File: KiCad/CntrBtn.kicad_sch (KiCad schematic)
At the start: 3 parts

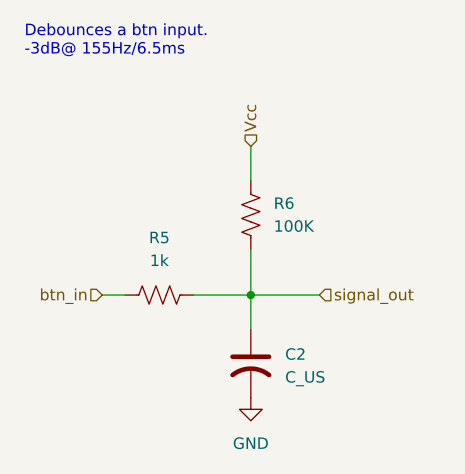
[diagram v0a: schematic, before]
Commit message: redid button pull up. Added initial joystick and display symbols
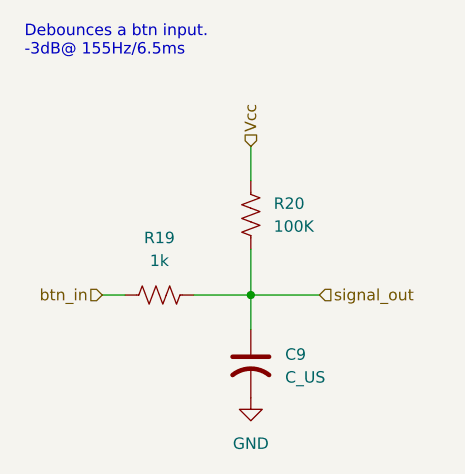
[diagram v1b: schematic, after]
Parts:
- renumbered C2 to C9, R5 to R19, R6 to R20
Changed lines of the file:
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@@
 		(dnp no)
 		(fields_autoplaced yes)
-		(property "Reference" "R5"
+		(property "Reference" "R19"
 			(at 38.1 45.72 90)
 			(effects
@@
 		(instances
 			(project "sb_handheld"
-				(path "/e2b47f54-afd4-414f-8c8f-251eedeb980e/77aafe8f-860d-4135-993b-3f03c481f100"
-					(reference "R5")
-					(unit 1)
-				)
 				(path "/e2b47f54-afd4-414f-8c8f-251eedeb980e/35c94761-efac-418a-91db-c9b83c0b3899/080458a5-8993-446e-83d9-bcde56d7c9a2"
 					(reference "R29")
@@
 				(path "/e2b47f54-afd4-414f-8c8f-251eedeb980e/35c94761-efac-418a-91db-c9b83c0b3899/f76cda86-381c-44b3-a7df-58f7c58efb05"
 					(reference "R31")
-					(unit 1)
-				)
-				(path "/e2b47f54-afd4-414f-8c8f-251eedeb980e/6239e351-1e9b-4e1a-998c-979da75b2bd8/2192cc8f-655d-4541-b277-b7a0a5260346"
-					(reference "R9")
-					(unit 1)
-				)
-				(path "/e2b47f54-afd4-414f-8c8f-251eedeb980e/6239e351-1e9b-4e1a-998c-979da75b2bd8/57806a10-d03e-45c2-905e-9ef24d9fc5a3"
-					(reference "R11")
-					(unit 1)
-				)
-				(path "/e2b47f54-afd4-414f-8c8f-251eedeb980e/6239e351-1e9b-4e1a-998c-979da75b2bd8/8ca35cf0-ef30-4af4-8c04-dbe73795e853"
-					(reference "R15")
-					(unit 1)
-				)
-				(path "/e2b47f54-afd4-414f-8c8f-251eedeb980e/6239e351-1e9b-4e1a-998c-979da75b2bd8/b6250329-bdc4-45c1-a6bb-2e0cadeb9f26"
-					(reference "R3")
-					(unit 1)
-				)
-				(path "/e2b47f54-afd4-414f-8c8f-251eedeb980e/6239e351-1e9b-4e1a-998c-979da75b2bd8/b65d468b-0271-475b-bfa0-5edddf91c73b"
-					(reference "R7")
-					(unit 1)
-				)
-				(path "/e2b47f54-afd4-414f-8c8f-251eedeb980e/6239e351-1e9b-4e1a-998c-979da75b2bd8/d2f4d4b1-81b0-4a1b-a44d-4fb0a202ecbb"
-					(reference "R17")
-					(unit 1)
-				)
-				(path "/e2b47f54-afd4-414f-8c8f-251eedeb980e/6239e351-1e9b-4e1a-998c-979da75b2bd8/d48abaaa-9c99-46dc-846f-bb3c471b4c2c"
-					(reference "R13")
 					(unit 1)
 				)
@@
 		(dnp no)
 		(fields_autoplaced yes)
-		(property "Reference" "#PWR030"
+		(property "Reference" "#PWR067"
 			(at 48.26 69.85 0)
 			(effects
@@
 		(instances
 			(project "sb_handheld"
-				(path "/e2b47f54-afd4-414f-8c8f-251eedeb980e/77aafe8f-860d-4135-993b-3f03c481f100"
-					(reference "#PWR030")
-					(unit 1)
-				)
 				(path "/e2b47f54-afd4-414f-8c8f-251eedeb980e/35c94761-efac-418a-91db-c9b83c0b3899/080458a5-8993-446e-83d9-bcde56d7c9a2"
 					(reference "#PWR072")
@@
 				(path "/e2b47f54-afd4-414f-8c8f-251eedeb980e/35c94761-efac-418a-91db-c9b83c0b3899/f76cda86-381c-44b3-a7df-58f7c58efb05"
 					(reference "#PWR073")
-					(unit 1)
-				)
-				(path "/e2b47f54-afd4-414f-8c8f-251eedeb980e/6239e351-1e9b-4e1a-998c-979da75b2bd8/2192cc8f-655d-4541-b277-b7a0a5260346"
-					(reference "#PWR034")
-					(unit 1)
-				)
-				(path "/e2b47f54-afd4-414f-8c8f-251eedeb980e/6239e351-1e9b-4e1a-998c-979da75b2bd8/57806a10-d03e-45c2-905e-9ef24d9fc5a3"
-					(reference "#PWR038")
-					(unit 1)
-				)
-				(path "/e2b47f54-afd4-414f-8c8f-251eedeb980e/6239e351-1e9b-4e1a-998c-979da75b2bd8/8ca35cf0-ef30-4af4-8c04-dbe73795e853"
-					(reference "#PWR042")
-					(unit 1)
-				)
-				(path "/e2b47f54-afd4-414f-8c8f-251eedeb980e/6239e351-1e9b-4e1a-998c-979da75b2bd8/b6250329-bdc4-45c1-a6bb-2e0cadeb9f26"
-					(reference "#PWR035")
-					(unit 1)
-				)
-				(path "/e2b47f54-afd4-414f-8c8f-251eedeb980e/6239e351-1e9b-4e1a-998c-979da75b2bd8/b65d468b-0271-475b-bfa0-5edddf91c73b"
-					(reference "#PWR032")
-					(unit 1)
-				)
-				(path "/e2b47f54-afd4-414f-8c8f-251eedeb980e/6239e351-1e9b-4e1a-998c-979da75b2bd8/d2f4d4b1-81b0-4a1b-a44d-4fb0a202ecbb"
-					(reference "#PWR044")
-					(unit 1)
-				)
-				(path "/e2b47f54-afd4-414f-8c8f-251eedeb980e/6239e351-1e9b-4e1a-998c-979da75b2bd8/d48abaaa-9c99-46dc-846f-bb3c471b4c2c"
-					(reference "#PWR040")
 					(unit 1)
 				)
@@
 		(dnp no)
 		(fields_autoplaced yes)
-		(property "Reference" "R6"
+		(property "Reference" "R20"
 			(at 50.8 41.9099 0)
 			(effects
@@
 		(instances
 			(project "sb_handheld"
-				(path "/e2b47f54-afd4-414f-8c8f-251eedeb980e/77aafe8f-860d-4135-993b-3f03c481f100"
-					(reference "R6")
-					(unit 1)
-				)
 				(path "/e2b47f54-afd4-414f-8c8f-251eedeb980e/35c94761-efac-418a-91db-c9b83c0b3899/080458a5-8993-446e-83d9-bcde56d7c9a2"
 					(reference "R30")
@@
 				(path "/e2b47f54-afd4-414f-8c8f-251eedeb980e/35c94761-efac-418a-91db-c9b83c0b3899/f76cda86-381c-44b3-a7df-58f7c58efb05"
 					(reference "R32")
-					(unit 1)
-				)
-				(path "/e2b47f54-afd4-414f-8c8f-251eedeb980e/6239e351-1e9b-4e1a-998c-979da75b2bd8/2192cc8f-655d-4541-b277-b7a0a5260346"
-					(reference "R10")
-					(unit 1)
-				)
-				(path "/e2b47f54-afd4-414f-8c8f-251eedeb980e/6239e351-1e9b-4e1a-998c-979da75b2bd8/57806a10-d03e-45c2-905e-9ef24d9fc5a3"
-					(reference "R12")
-					(unit 1)
-				)
-				(path "/e2b47f54-afd4-414f-8c8f-251eedeb980e/6239e351-1e9b-4e1a-998c-979da75b2bd8/8ca35cf0-ef30-4af4-8c04-dbe73795e853"
-					(reference "R16")
-					(unit 1)
-				)
-				(path "/e2b47f54-afd4-414f-8c8f-251eedeb980e/6239e351-1e9b-4e1a-998c-979da75b2bd8/b6250329-bdc4-45c1-a6bb-2e0cadeb9f26"
-					(reference "R4")
-					(unit 1)
-				)
-				(path "/e2b47f54-afd4-414f-8c8f-251eedeb980e/6239e351-1e9b-4e1a-998c-979da75b2bd8/b65d468b-0271-475b-bfa0-5edddf91c73b"
-					(reference "R8")
-					(unit 1)
-				)
-				(path "/e2b47f54-afd4-414f-8c8f-251eedeb980e/6239e351-1e9b-4e1a-998c-979da75b2bd8/d2f4d4b1-81b0-4a1b-a44d-4fb0a202ecbb"
-					(reference "R18")
-					(unit 1)
-				)
-				(path "/e2b47f54-afd4-414f-8c8f-251eedeb980e/6239e351-1e9b-4e1a-998c-979da75b2bd8/d48abaaa-9c99-46dc-846f-bb3c471b4c2c"
-					(reference "R14")
 					(unit 1)
 				)
@@
 		(dnp no)
 		(fields_autoplaced yes)
-		(property "Reference" "C2"
+		(property "Reference" "C9"
 			(at 52.07 58.6739 0)
 			(effects
@@
 		(instances
 			(project "sb_handheld"
-				(path "/e2b47f54-afd4-414f-8c8f-251eedeb980e/77aafe8f-860d-4135-993b-3f03c481f100"
-					(reference "C2")
-					(unit 1)
-				)
 				(path "/e2b47f54-afd4-414f-8c8f-251eedeb980e/35c94761-efac-418a-91db-c9b83c0b3899/080458a5-8993-446e-83d9-bcde56d7c9a2"
 					(reference "C14")
@@
 					(unit 1)
 				)
-				(path "/e2b47f54-afd4-414f-8c8f-251eedeb980e/6239e351-1e9b-4e1a-998c-979da75b2bd8/2192cc8f-655d-4541-b277-b7a0a5260346"
-					(reference "C4")
-					(unit 1)
-				)
-				(path "/e2b47f54-afd4-414f-8c8f-251eedeb980e/6239e351-1e9b-4e1a-998c-979da75b2bd8/57806a10-d03e-45c2-905e-9ef24d9fc5a3"
-					(reference "C5")
-					(unit 1)
-				)
-				(path "/e2b47f54-afd4-414f-8c8f-251eedeb980e/6239e351-1e9b-4e1a-998c-979da75b2bd8/8ca35cf0-ef30-4af4-8c04-dbe73795e853"
-					(reference "C7")
-					(unit 1)
-				)
-				(path "/e2b47f54-afd4-414f-8c8f-251eedeb980e/6239e351-1e9b-4e1a-998c-979da75b2bd8/b6250329-bdc4-45c1-a6bb-2e0cadeb9f26"
-					(reference "C1")
-					(unit 1)
-				)
-				(path "/e2b47f54-afd4-414f-8c8f-251eedeb980e/6239e351-1e9b-4e1a-998c-979da75b2bd8/b65d468b-0271-475b-bfa0-5edddf91c73b"
-					(reference "C3")
-					(unit 1)
-				)
-				(path "/e2b47f54-afd4-414f-8c8f-251eedeb980e/6239e351-1e9b-4e1a-998c-979da75b2bd8/d2f4d4b1-81b0-4a1b-a44d-4fb0a202ecbb"
-					(reference "C8")
-					(unit 1)
-				)
-				(path "/e2b47f54-afd4-414f-8c8f-251eedeb980e/6239e351-1e9b-4e1a-998c-979da75b2bd8/d48abaaa-9c99-46dc-846f-bb3c471b4c2c"
-					(reference "C6")
-					(unit 1)
-				)
